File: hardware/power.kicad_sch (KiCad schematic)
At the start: 12 parts, among them J1 USB-C, J2 5V in, J6 SWD, SW1 BOOTSEL, SW2 RESET, U4 USBLC6-2SC6

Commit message: PCB rev 0.2: RP2350B on the board instead of the PGA2350 module
The PGA2350 is replaced by an RP2350B with Raspberry Pi's minimal-design
support circuit: their core regulator (polarity-marked inductor), 12 MHz
crystal, W25Q128 flash and USB 27R, with their regulator, QSPI and USB
layout copied relative to the VREG_LX pin; an AMS1117 makes 3V3. GPIO
numbers are unchanged. Supply pins each have a via under the chip.

Cheaper parts from the HDD Synth Mk5: HRO TYPE-C-31-M-12 USB-C, TS-1187A
buttons, and a generic TF PUSH microSD socket. The CB3T3245 bus switches
stay. Every symbol carries its LCSC part number, and Fabrication Toolkit
offsets where JLCPCB's footprint differs from KiCad's; jlcpcb.py applies
the same fitted corrections. check_netlist.py also checks the RP2350
support circuit. ERC and DRC are clean; parts for 5 boards about $68.50.

Co-Authored-By: Claude Opus 5.5 <noreply@anthropic.com>
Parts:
- added C29: 10uF, Capacitor_SMD:C_0805_2012Metric, symbol Device:C
- added U8: AMS1117-3.3, Package_TO_SOT_SMD:SOT-223-3_TabPin2, symbol Regulator_Linear:AMS1117-3.3
- C1: LCSC (none) -> C15850
- D1, D2: LCSC (none) -> C2480
- F1: LCSC (none) -> C19193043
- J1: footprint Connector_USB:USB_C_Receptacle_GCT_USB4105-xx-A_16P_TopMnt_Horizontal -> Connector_USB:USB_C_Receptacle_HRO_TYPE-C-31-M-12; FT Position Offset (none) -> 0,0.111; LCSC (none) -> C165948; MPN GCT USB4105-GF-A-120 -> HRO TYPE-C-31-M-12
- J2: FT Rotation Offset (none) -> 180; LCSC (none) -> C158012
- J6: FT Rotation Offset (none) -> -90; LCSC (none) -> C2937625
- R1, R2: LCSC (none) -> C23186
- SW1, SW2: footprint Button_Switch_SMD:SW_SPST_B3U-1000P -> Button_Switch_SMD:SW_Push_1P1T_XKB_TS-1187A; LCSC (none) -> C318884
- U4: FT Rotation Offset (none) -> 90; LCSC (none) -> C2687116
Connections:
- net GND: now also C29.2, U8.1 (GND)
- net VB: now also U8.3 (VI)
- net RUN renamed RUN_BTN
- new net +3V3: C29.1, U8.2 (VO)
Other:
- note added: "3V3 for everything: ~1 V dropout, so 3.3 V holds down to about 4.4 V on VB. The board draws well under 300 mA."
- note added: "ESD protection, close to J1. The 27 R series resistors sit by the RP2350 (RP2350 sheet)."
- note added: "Hold BOOTSEL and press RESET for the UF2 drive. Both go through 1k on the RP2350 sheet."
- note added: "USB-C (power and flashing) and the 5 V header, diode-ORed into VB; an AMS1117 makes 3V3 from it. Never connect the IDE adapter's 5 V (Molex) to this board: the boards share ground only."
- note removed: "ESD protection, close to J1. The module has the 27 R series resistors on D+/D-."
- note removed: "Hold BOOTSEL and press RESET for the UF2 drive."
- note removed: "USB-C (power and flashing) and the 5 V header, diode-ORed into the PGA2350's VBUS (VB). Never connect the IDE adapter's 5 V (Molex) to this board: the boards share ground only."

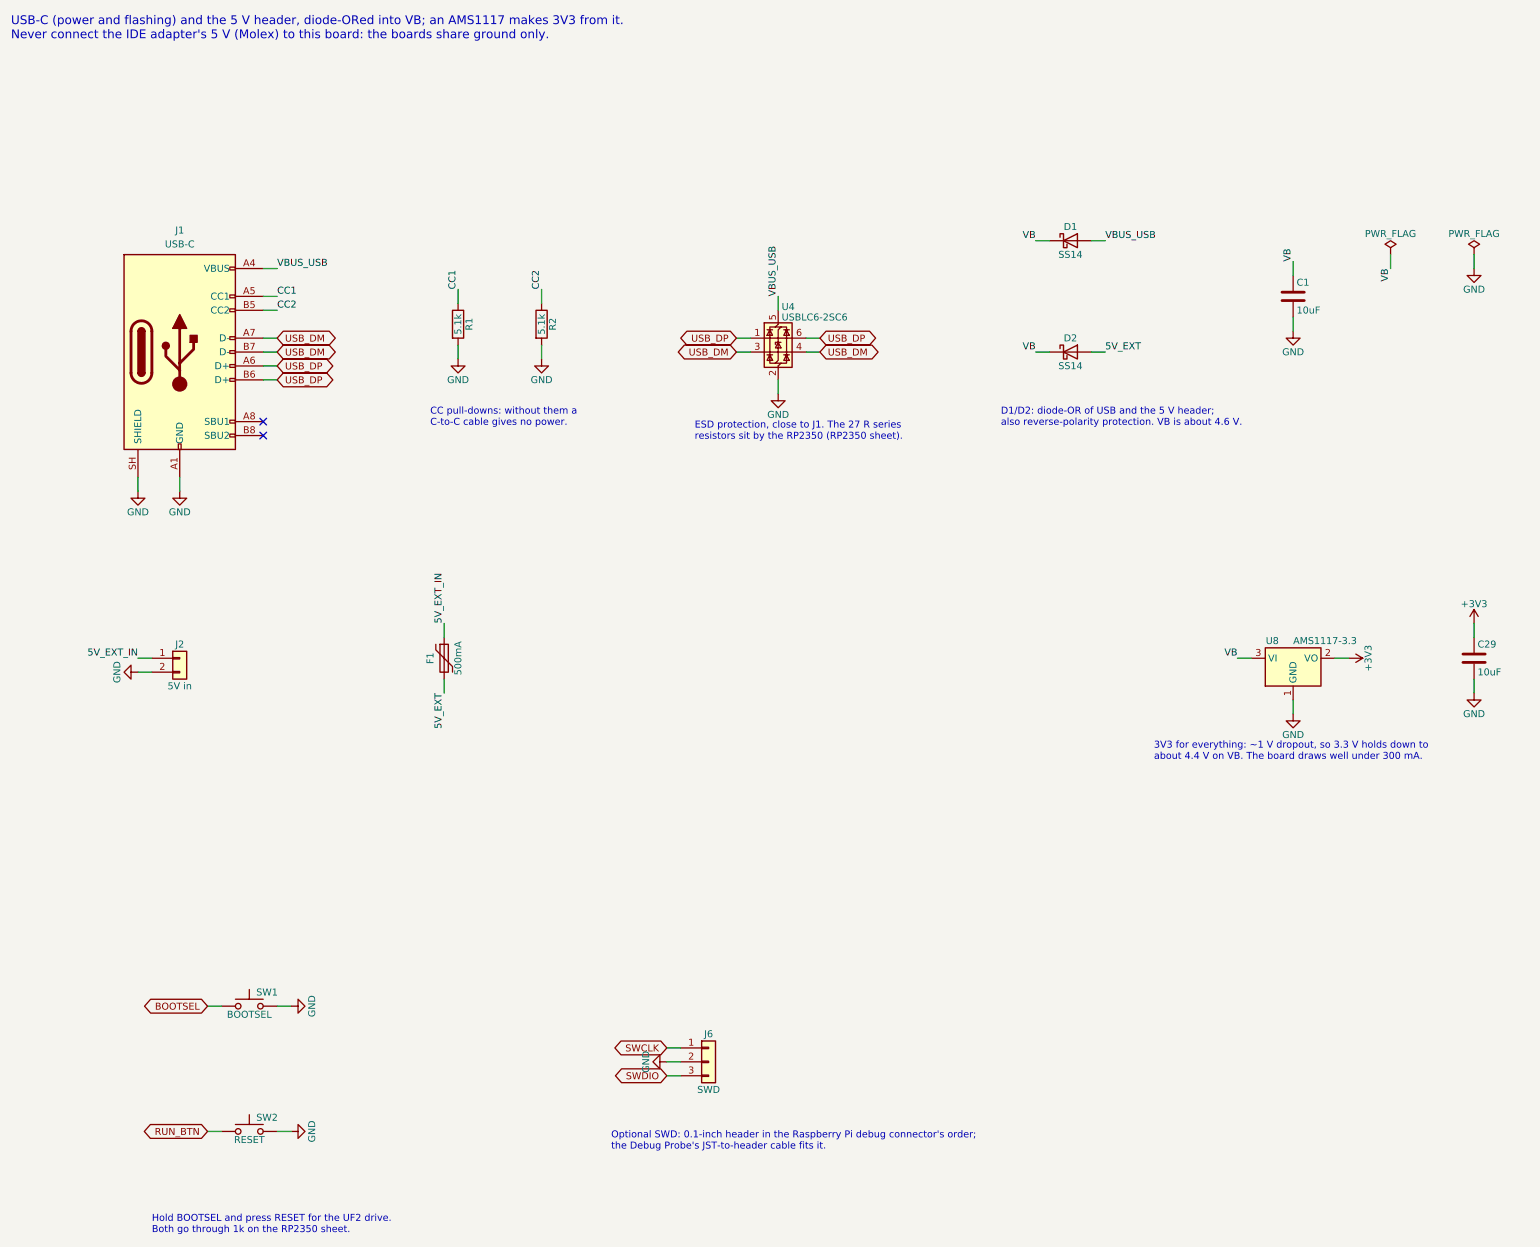
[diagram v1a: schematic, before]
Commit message: PCB rev 0.3: HDD Synth Mk5 outline and holes, 5 V in on the link socket
- The board takes the Mk5's outline (100.33 x 69.88 mm, 2.54 mm corners)
  and its four M3 holes, so the two boards stack on standoffs. The IDE
  header moves inside the left-hand holes; everything else shifts right.
  The logo still fits on the front.
- J3 pin 1 takes 5 V from the HDD Synth through D5 (SS14) into VB, beside
  USB and the 5 V header, so one supply can run both boards. The Mk5's J6
  pin 1 is 3.3 V, so leave it unconnected with a Mk5.
- check_netlist.py checks the new input; rerouted with Freerouting: ERC 0,
  DRC 0 errors, 0 unconnected, 0 parity issues.

Co-Authored-By: Claude Opus 5.5 <noreply@anthropic.com>
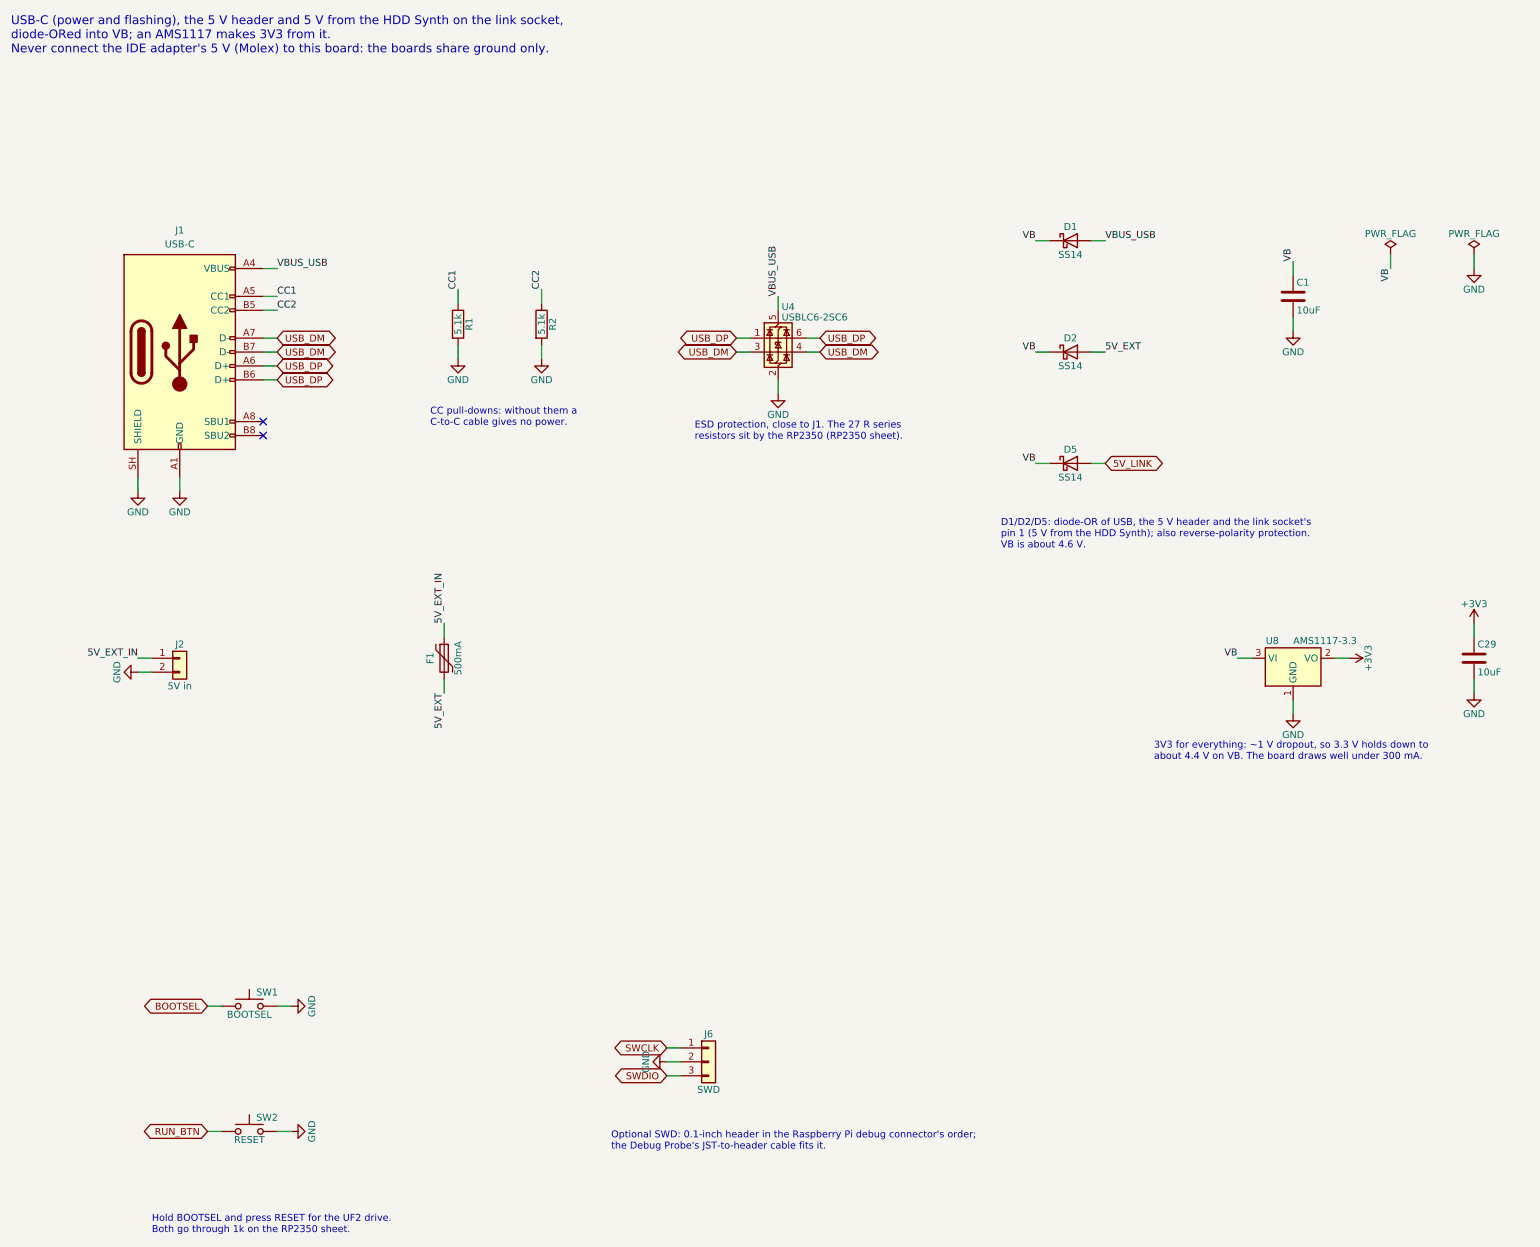
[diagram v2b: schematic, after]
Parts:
- added D5: SS14, Diode_SMD:D_SMA, symbol Device:D_Schottky
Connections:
- net VB: now also D5.1 (K)
- new net 5V_LINK: D5.2 (A)
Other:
- note added: "D1/D2/D5: diode-OR of USB, the 5 V header and the link socket's pin 1 (5 V from the HDD Synth); also reverse-polarity protection. VB is about 4.6 V."
- note added: "USB-C (power and flashing), the 5 V header and 5 V from the HDD Synth on the link socket, diode-ORed into VB; an AMS1117 makes 3V3 from it. Never connect the IDE adapter's 5 V (Molex) to this board: the boards share ground only."
- note removed: "D1/D2: diode-OR of USB and the 5 V header; also reverse-polarity protection. VB is about 4.6 V."
- note removed: "USB-C (power and flashing) and the 5 V header, diode-ORed into VB; an AMS1117 makes 3V3 from it. Never connect the IDE adapter's 5 V (Molex) to this board: the boards share ground only."
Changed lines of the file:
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@@
 	(title_block
 		(title "HDDSynthPro: Power and USB")
-		(date "2026-10-26")
-		(rev "0.1")
+		(date "2026-10-27")
+		(rev "0.3")
 		(company "HDDSynthPro")
 		(comment 1 "Generated by hardware/tools/gen_schematic.py from docs/pcb.html")
 	)
-	(text "USB-C (power and flashing) and the 5 V header, diode-ORed into VB; an AMS1117 makes 3V3 from it.\nNever connect the IDE adapter's 5 V (Molex) to this board: the boards share ground only."
+	(text "USB-C (power and flashing), the 5 V header and 5 V from the HDD Synth on the link socket,\ndiode-ORed into VB; an AMS1117 makes 3V3 from it.\nNever connect the IDE adapter's 5 V (Molex) to this board: the boards share ground only."
 		(exclude_from_sim no)
 		(at 20 20 0)
@@
 		)
 	)
-	(text "D1/D2: diode-OR of USB and the 5 V header;\nalso reverse-polarity protection. VB is about 4.6 V."
+	(symbol
+		(lib_id "Device:D_Schottky")
+		(at 213.36 101.6 0)
+		(unit 1)
 		(exclude_from_sim no)
-		(at 200.66 91.44 0)
+		(in_bom yes)
+		(on_board yes)
+		(dnp no)
+		(property "Reference" "D5"
+			(at 213.36 99.06 0)
+			(effects
+				(font
+					(size 1.27 1.27)
+				)
+			)
+		)
+		(property "Value" "SS14"
+			(at 213.36 104.14 0)
+			(effects
+				(font
+					(size 1.27 1.27)
+				)
+			)
+		)
+		(property "Footprint" "Diode_SMD:D_SMA"
+			(at 213.36 101.6 0)
+			(effects
+				(font
+					(size 1.27 1.27)
+				)
+				(hide yes)
+			)
+		)
+		(property "Datasheet" ""
+			(at 213.36 101.6 0)
+			(effects
+				(font
+					(size 1.27 1.27)
+				)
+				(hide yes)
+			)
+		)
+		(property "Description" "Schottky diode"
+			(at 213.36 101.6 0)
+			(effects
+				(font
+					(size 1.27 1.27)
+				)
+				(hide yes)
+			)
+		)
+		(property "LCSC" "C2480"
+			(at 213.36 101.6 0)
+			(effects
+				(font
+					(size 1.27 1.27)
+				)
+				(hide yes)
+			)
+		)
+		(pin "1"
+		)
+		(pin "2"
+		)
+		(instances
+			(project "hddsynthpro"
+				(path "/1f1928de-57c1-5ffb-9b24-ae415e42f504/6a60ff82-27b4-567a-b4d6-c1b6fcfcc09c"
+					(reference "D5")
+					(unit 1)
+				)
+			)
+		)
+	)
+	(wire
+		(pts
+			(xy 209.55 101.6)
+			(xy 207.01 101.6)
+		)
+		(stroke
+			(width 0)
+			(type default)
+		)
+	)
+	(wire
+		(pts
+			(xy 217.17 101.6)
+			(xy 219.71 101.6)
+		)
+		(stroke
+			(width 0)
+			(type default)
+		)
+	)
+	(text "D1/D2/D5: diode-OR of USB, the 5 V header and the link socket's\npin 1 (5 V from the HDD Synth); also reverse-polarity protection.\nVB is about 4.6 V."
+		(exclude_from_sim no)
+		(at 200.66 111.76 0)
 		(effects
 			(font
@@
 		)
 	)
+	(label "VB"
+		(at 207.01 101.6 180)
+		(fields_autoplaced yes)
+		(effects
+			(font
+				(size 1.27 1.27)
+			)
+			(justify right bottom)
+		)
+	)
+	(global_label "5V_LINK"
+		(shape bidirectional)
+		(at 219.71 101.6 0)
+		(fields_autoplaced yes)
+		(effects
+			(font
+				(size 1.27 1.27)
+			)
+			(justify left)
+		)
+		(property "Intersheetrefs" "${INTERSHEET_REFS}"
+			(at 219.71 101.6 0)
+			(effects
+				(font
+					(size 1.27 1.27)
+				)
+				(justify left)
+				(hide yes)
+			)
+		)
+	)
